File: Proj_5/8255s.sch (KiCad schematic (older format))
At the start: 18 parts, among them J1 Conn_02x15_Top_Bottom, J2 Conn_02x15_Top_Bottom, J3 Conn_02x15_Top_Bottom, U1 8255, U2 8255, U3 8255, U39 74LVC1G11, U40 74LVC1G11, U41 74AHC1G08, U42 74LVC1G11, U43 74AHC1G08, U44 74LVC1G11, U45 74AHC1G08, U46 74LVC1G11, U47 PAL16L8

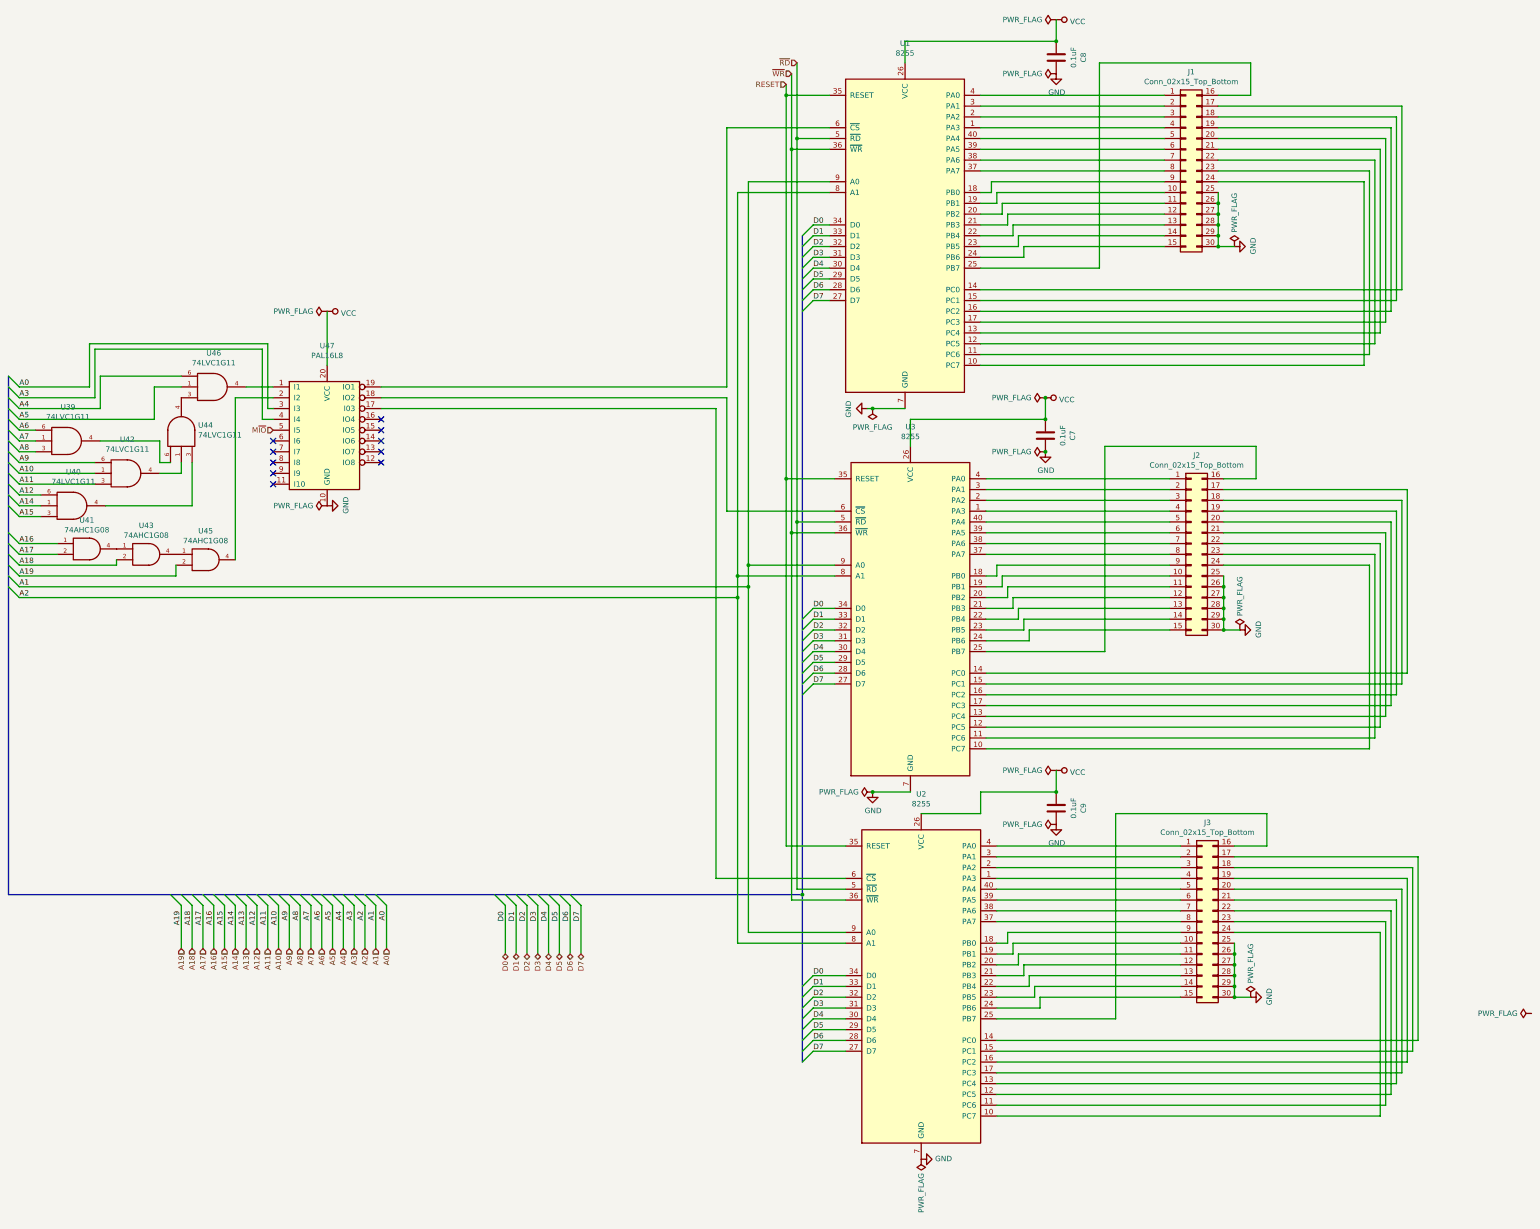
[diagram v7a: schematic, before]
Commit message: Power Flags
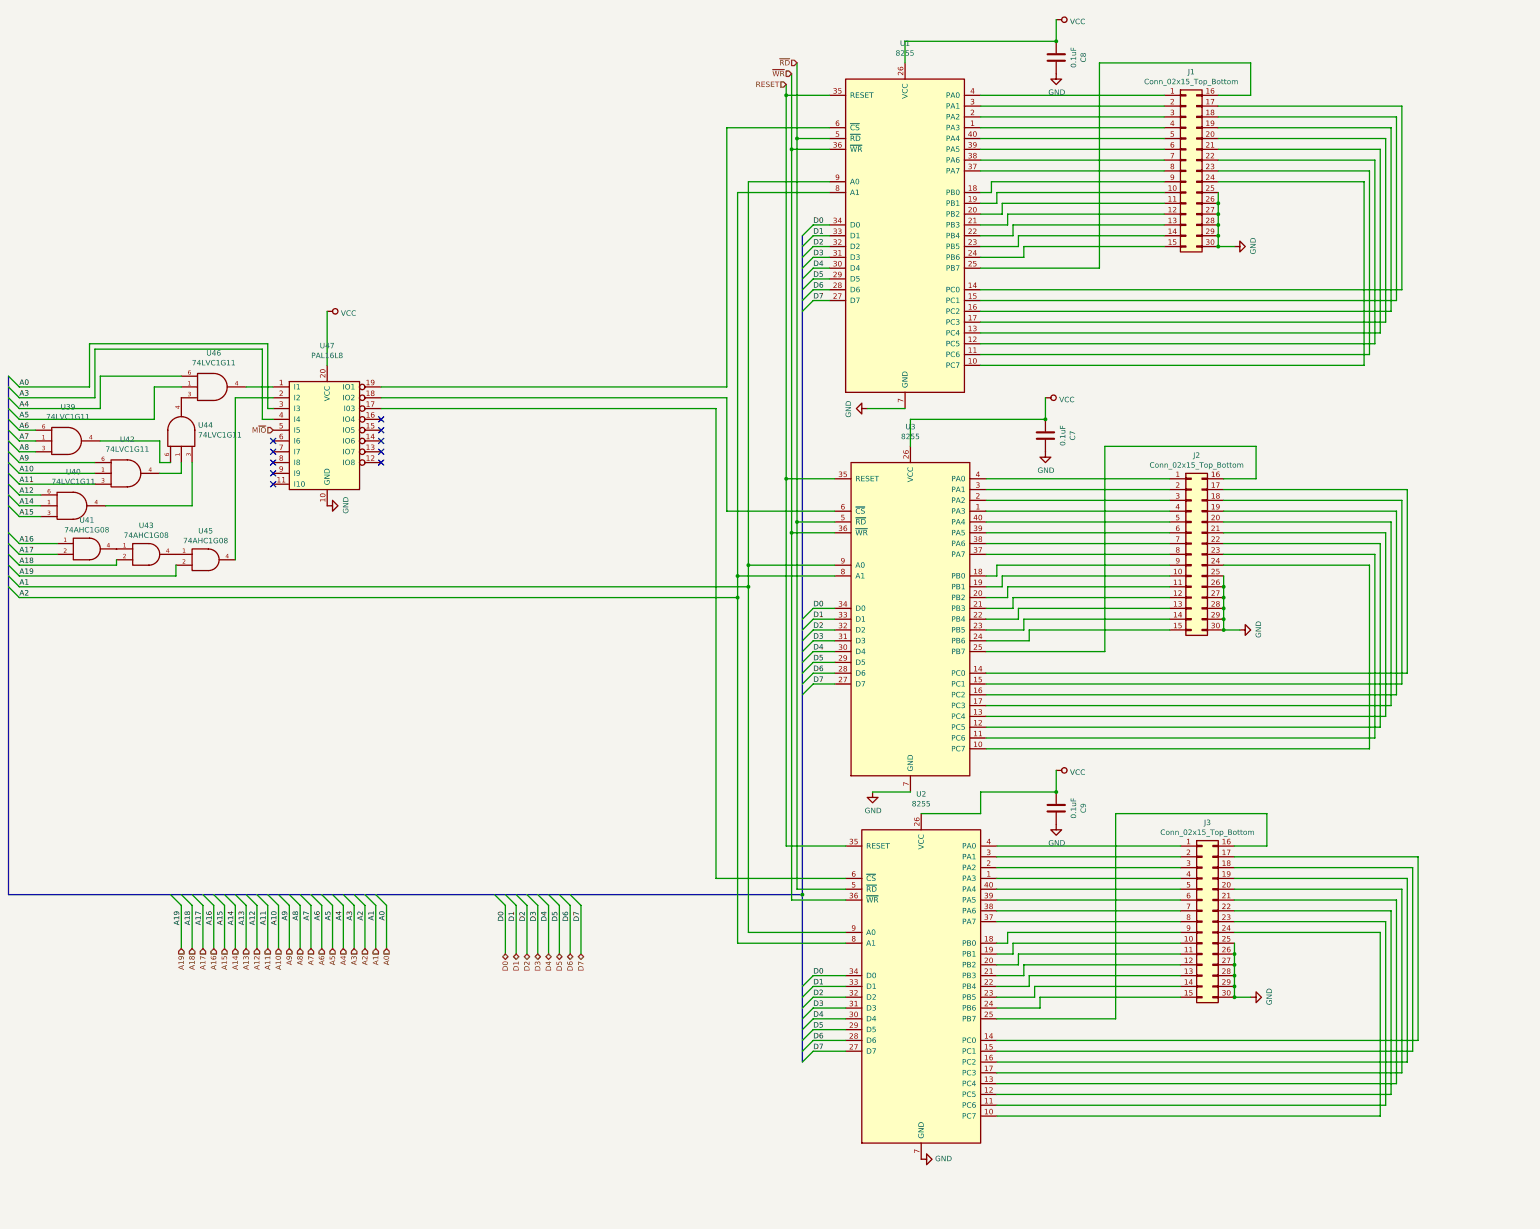
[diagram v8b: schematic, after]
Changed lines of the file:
@@
 $Descr A2 23386 16535
 encoding utf-8
-Sheet 6 10
+Sheet 5 10
 Title ""
 Date ""
@@
 	1    0    0    -1
 $EndComp
-$Comp
-L power:PWR_FLAG #FLG?
-U 1 1 5F9D6E5F
-P 9150 11150
-AR Path="/5EAF7226/5F9D6E5F" Ref="#FLG?"  Part="1"
-AR Path="/5EA0416B/5F9D6E5F" Ref="#FLG049"  Part="1"
-F 0 "#FLG049" H 9150 11225 50  0001 C CNN
-F 1 "PWR_FLAG" V 9150 11278 50  0000 L CNN
-F 2 "" H 9150 11150 50  0001 C CNN
-F 3 "~" H 9150 11150 50  0001 C CNN
-	1    9150 11150
-	-1   0    0    1
-$EndComp
 Connection ~ 10400 7750
-$Comp
-L power:PWR_FLAG #FLG?
-U 1 1 5FABCA41
-P 10400 7550
-AR Path="/5EAF7226/5FABCA41" Ref="#FLG?"  Part="1"
-AR Path="/5EA0416B/5FABCA41" Ref="#FLG054"  Part="1"
-F 0 "#FLG054" H 10400 7625 50  0001 C CNN
-F 1 "PWR_FLAG" V 10400 7678 50  0000 L CNN
-F 2 "" H 10400 7550 50  0001 C CNN
-F 3 "~" H 10400 7550 50  0001 C CNN
-	1    10400 7550
-	0    -1   -1   0
-$EndComp
-$Comp
-L power:PWR_FLAG #FLG?
-U 1 1 5FAD9013
-P 10400 8050
-AR Path="/5EAF7226/5FAD9013" Ref="#FLG?"  Part="1"
-AR Path="/5EA0416B/5FAD9013" Ref="#FLG055"  Part="1"
-F 0 "#FLG055" H 10400 8125 50  0001 C CNN
-F 1 "PWR_FLAG" V 10400 8178 50  0000 L CNN
-F 2 "" H 10400 8050 50  0001 C CNN
-F 3 "~" H 10400 8050 50  0001 C CNN
-	1    10400 8050
-	0    -1   -1   0
-$EndComp
-$Comp
-L power:PWR_FLAG #FLG?
-U 1 1 5FB660D7
-P 8700 7750
-AR Path="/5EAF7226/5FB660D7" Ref="#FLG?"  Part="1"
-AR Path="/5EA0416B/5FB660D7" Ref="#FLG048"  Part="1"
-F 0 "#FLG048" H 8700 7825 50  0001 C CNN
-F 1 "PWR_FLAG" V 8700 7878 50  0000 L CNN
-F 2 "" H 8700 7750 50  0001 C CNN
-F 3 "~" H 8700 7750 50  0001 C CNN
-	1    8700 7750
-	0    -1   -1   0
-$EndComp
 Wire Wire Line
 	9050 7750 8700 7750
-Connection ~ 8700 7750
 Wire Wire Line
 	9150 7950 9700 7950
@@
 Connection ~ 10300 4300
 $Comp
-L power:PWR_FLAG #FLG?
-U 1 1 5FBF3490
-P 10300 4100
-AR Path="/5EAF7226/5FBF3490" Ref="#FLG?"  Part="1"
-AR Path="/5EA0416B/5FBF3490" Ref="#FLG050"  Part="1"
-F 0 "#FLG050" H 10300 4175 50  0001 C CNN
-F 1 "PWR_FLAG" V 10300 4228 50  0000 L CNN
-F 2 "" H 10300 4100 50  0001 C CNN
-F 3 "~" H 10300 4100 50  0001 C CNN
-	1    10300 4100
-	0    -1   -1   0
-$EndComp
-$Comp
-L power:PWR_FLAG #FLG?
-U 1 1 5FBF3496
-P 10300 4600
-AR Path="/5EAF7226/5FBF3496" Ref="#FLG?"  Part="1"
-AR Path="/5EA0416B/5FBF3496" Ref="#FLG051"  Part="1"
-F 0 "#FLG051" H 10300 4675 50  0001 C CNN
-F 1 "PWR_FLAG" V 10300 4728 50  0000 L CNN
-F 2 "" H 10300 4600 50  0001 C CNN
-F 3 "~" H 10300 4600 50  0001 C CNN
-	1    10300 4600
-	0    -1   -1   0
-$EndComp
-Connection ~ 10300 4100
-Connection ~ 10300 4600
-$Comp
 L Device:C C8
 U 1 1 5FC65F6F
@@
 $EndComp
 Connection ~ 10400 800
-$Comp
-L power:PWR_FLAG #FLG?
-U 1 1 5FC65F83
-P 10400 600
-AR Path="/5EAF7226/5FC65F83" Ref="#FLG?"  Part="1"
-AR Path="/5EA0416B/5FC65F83" Ref="#FLG052"  Part="1"
-F 0 "#FLG052" H 10400 675 50  0001 C CNN
-F 1 "PWR_FLAG" V 10400 728 50  0000 L CNN
-F 2 "" H 10400 600 50  0001 C CNN
-F 3 "~" H 10400 600 50  0001 C CNN
-	1    10400 600
-	0    -1   -1   0
-$EndComp
-$Comp
-L power:PWR_FLAG #FLG?
-U 1 1 5FC65F89
-P 10400 1100
-AR Path="/5EAF7226/5FC65F89" Ref="#FLG?"  Part="1"
-AR Path="/5EA0416B/5FC65F89" Ref="#FLG053"  Part="1"
-F 0 "#FLG053" H 10400 1175 50  0001 C CNN
-F 1 "PWR_FLAG" V 10400 1228 50  0000 L CNN
-F 2 "" H 10400 1100 50  0001 C CNN
-F 3 "~" H 10400 1100 50  0001 C CNN
-	1    10400 1100
-	0    -1   -1   0
-$EndComp
 Wire Wire Line
 	9000 800  9000 1000
@@
 	9000 800  10400 800
 Wire Wire Line
-	9000 4200 8700 4200
-$Comp
-L power:PWR_FLAG #FLG?
-U 1 1 5FD0FE94
-P 8700 4200
-AR Path="/5EAF7226/5FD0FE94" Ref="#FLG?"  Part="1"
-AR Path="/5EA0416B/5FD0FE94" Ref="#FLG047"  Part="1"
-F 0 "#FLG047" H 8700 4275 50  0001 C CNN
-F 1 "PWR_FLAG" H 8700 4373 50  0000 C CNN
-F 2 "" H 8700 4200 50  0001 C CNN
-F 3 "~" H 8700 4200 50  0001 C CNN
-	1    8700 4200
-	-1   0    0    1
-$EndComp
-Connection ~ 8700 4200
-Wire Wire Line
-	8700 4200 8650 4200
-Wire Wire Line
 	9050 4300 9050 4550
 Wire Wire Line
 	9050 4300 10300 4300
-$Comp
-L power:PWR_FLAG #FLG?
-U 1 1 5FD2F941
-P 14800 9800
-AR Path="/5EAF7226/5FD2F941" Ref="#FLG?"  Part="1"
-AR Path="/5EA0416B/5FD2F941" Ref="#FLG059"  Part="1"
-F 0 "#FLG059" H 14800 9875 50  0001 C CNN
-F 1 "PWR_FLAG" V 14800 9928 50  0000 L CNN
-F 2 "" H 14800 9800 50  0001 C CNN
-F 3 "~" H 14800 9800 50  0001 C CNN
-	1    14800 9800
-	0    -1   -1   0
-$EndComp
-$Comp
-L power:PWR_FLAG #FLG?
-U 1 1 5FD857DB
-P 12200 9650
-AR Path="/5EAF7226/5FD857DB" Ref="#FLG?"  Part="1"
-AR Path="/5EA0416B/5FD857DB" Ref="#FLG058"  Part="1"
-F 0 "#FLG058" H 12200 9725 50  0001 C CNN
-F 1 "PWR_FLAG" V 12200 9778 50  0000 L CNN
-F 2 "" H 12200 9650 50  0001 C CNN
-F 3 "~" H 12200 9650 50  0001 C CNN
-	1    12200 9650
-	1    0    0    -1
-$EndComp
-$Comp
-L power:PWR_FLAG #FLG?
-U 1 1 5FDA22C7
-P 12100 6250
-AR Path="/5EAF7226/5FDA22C7" Ref="#FLG?"  Part="1"
-AR Path="/5EA0416B/5FDA22C7" Ref="#FLG057"  Part="1"
-F 0 "#FLG057" H 12100 6325 50  0001 C CNN
-F 1 "PWR_FLAG" V 12100 6378 50  0000 L CNN
-F 2 "" H 12100 6250 50  0001 C CNN
-F 3 "~" H 12100 6250 50  0001 C CNN
-	1    12100 6250
-	1    0    0    -1
-$EndComp
-$Comp
-L power:PWR_FLAG #FLG?
-U 1 1 5FDBEA5A
-P 12050 2700
-AR Path="/5EAF7226/5FDBEA5A" Ref="#FLG?"  Part="1"
-AR Path="/5EA0416B/5FDBEA5A" Ref="#FLG056"  Part="1"
-F 0 "#FLG056" H 12050 2775 50  0001 C CNN
-F 1 "PWR_FLAG" V 12050 2828 50  0000 L CNN
-F 2 "" H 12050 2700 50  0001 C CNN
-F 3 "~" H 12050 2700 50  0001 C CNN
-	1    12050 2700
-	1    0    0    -1
-$EndComp
-$Comp
-L power:PWR_FLAG #FLG?
-U 1 1 5FDDBCDC
-P 3650 5100
-AR Path="/5EAF7226/5FDDBCDC" Ref="#FLG?"  Part="1"
-AR Path="/5EA0416B/5FDDBCDC" Ref="#FLG046"  Part="1"
-F 0 "#FLG046" H 3650 5175 50  0001 C CNN
-F 1 "PWR_FLAG" V 3650 5228 50  0000 L CNN
-F 2 "" H 3650 5100 50  0001 C CNN
-F 3 "~" H 3650 5100 50  0001 C CNN
-	1    3650 5100
-	0    -1   -1   0
-$EndComp
 $Comp
 L power:VCC #PWR048
@@
 	0    1    1    0
 $EndComp
-$Comp
-L power:PWR_FLAG #FLG?
-U 1 1 5FDF952F
-P 3650 3300
-AR Path="/5EAF7226/5FDF952F" Ref="#FLG?"  Part="1"
-AR Path="/5EA0416B/5FDF952F" Ref="#FLG045"  Part="1"
-F 0 "#FLG045" H 3650 3375 50  0001 C CNN
-F 1 "PWR_FLAG" V 3650 3428 50  0000 L CNN
-F 2 "" H 3650 3300 50  0001 C CNN
-F 3 "~" H 3650 3300 50  0001 C CNN
-	1    3650 3300
-	0    -1   -1   0
-$EndComp
 Wire Wire Line
 	3650 3300 3650 3800
+Wire Wire Line
+	8650 4200 9000 4200
 Wire Bus Line
 	8050 8700 8050 10250
